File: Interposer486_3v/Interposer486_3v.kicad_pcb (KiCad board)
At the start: 2 copper layers, 48.3 x 52.1 mm, 170 parts, among them J1 WB/~WT, J2 CLKMUL

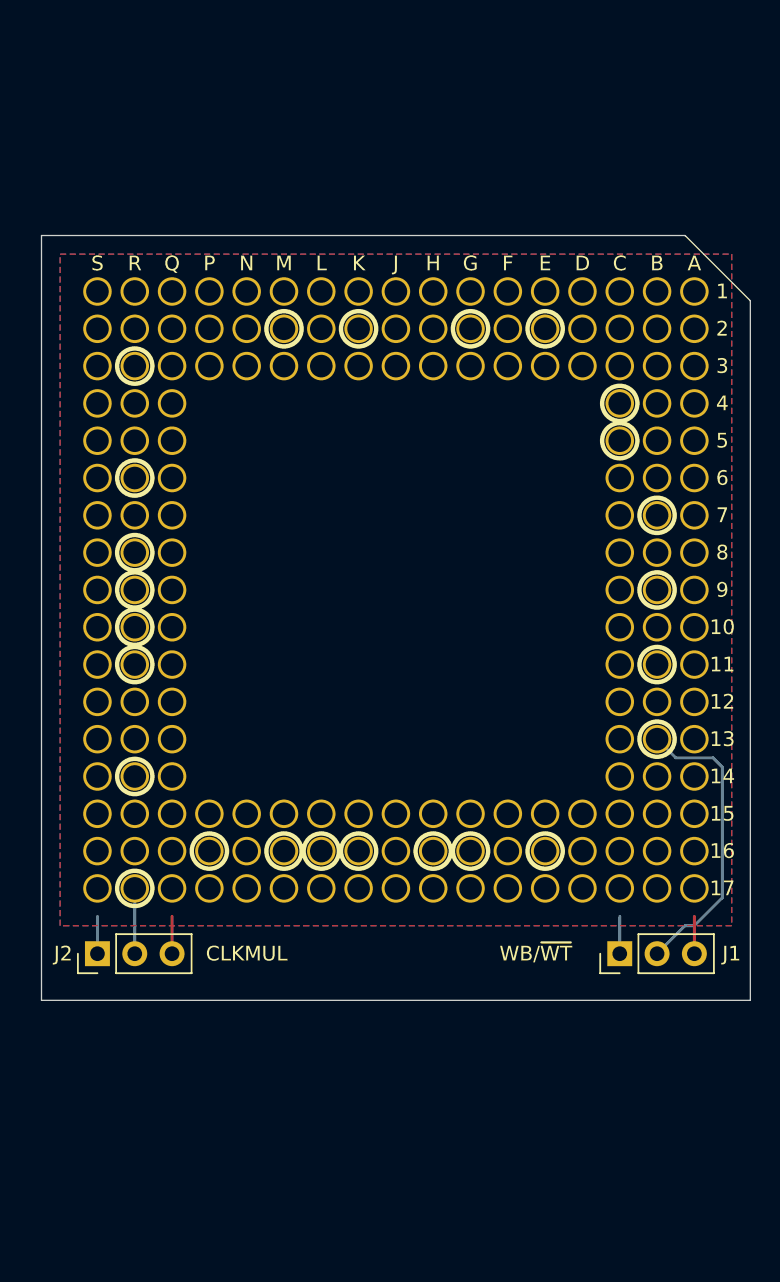
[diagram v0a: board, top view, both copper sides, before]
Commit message: Completed first pass of layout of 486 3v interposer.
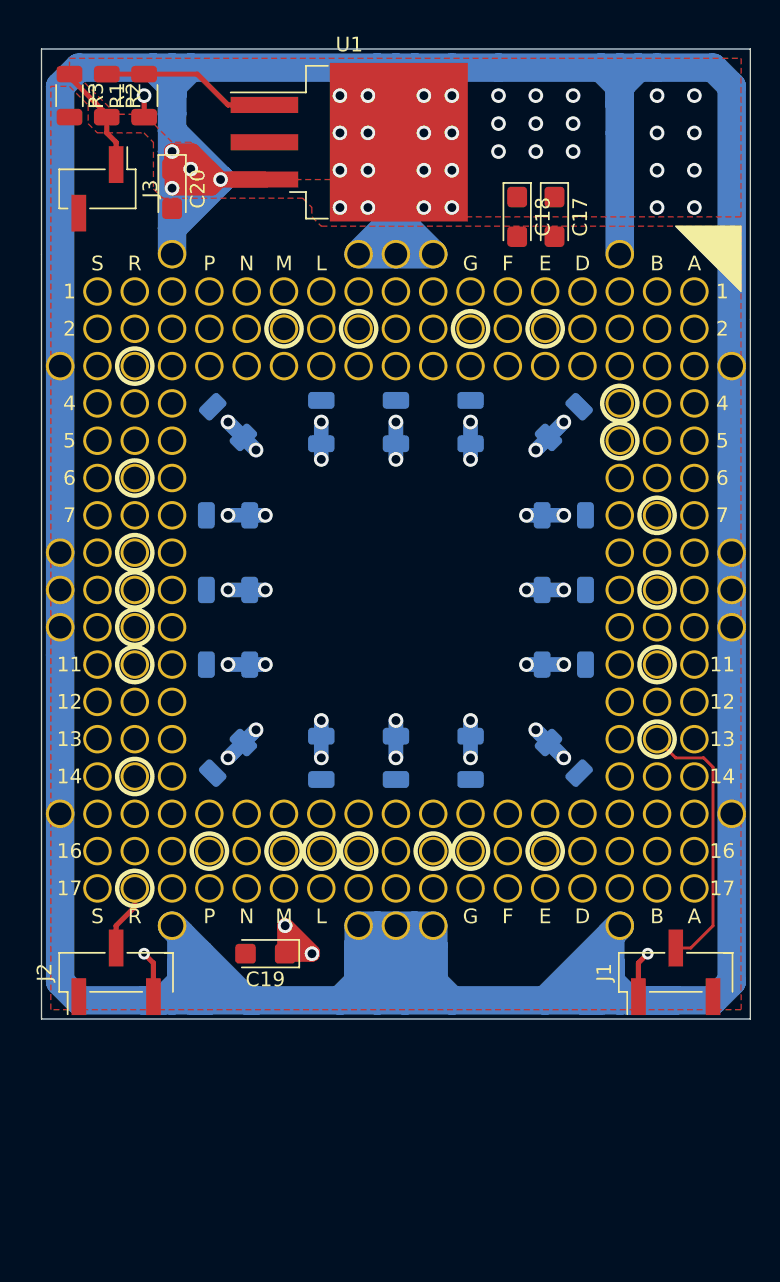
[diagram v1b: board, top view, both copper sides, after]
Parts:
- added C1: 0.1uF, Capacitor_SMD:C_1206_3216Metric, B.Cu at (146.1, 69.8)
- added C10: 0.1uF, Capacitor_SMD:C_1206_3216Metric, B.Cu at (162.6, 92.7)
- added C11: 0.1uF, Capacitor_SMD:C_1206_3216Metric, B.Cu at (157.5, 92.7)
- added C12: 0.1uF, Capacitor_SMD:C_1206_3216Metric, B.Cu at (152.4, 92.7)
- added C13: 0.1uF, Capacitor_SMD:C_1206_3216Metric, B.Cu at (146.1, 92.7)
- added C14: 0.1uF, Capacitor_SMD:C_1206_3216Metric, B.Cu at (146.1, 86.4)
- added C15: 0.1uF, Capacitor_SMD:C_1206_3216Metric, B.Cu at (146.1, 81.3)
- added C16: 0.1uF, Capacitor_SMD:C_1206_3216Metric, B.Cu at (146.1, 76.2)
- added C17: 10uF, Capacitor_Tantalum_SMD:CP_EIA-3216-10_Kemet-I, F.Cu at (168.3, 55.9)
- added C18: 10uF, Capacitor_Tantalum_SMD:CP_EIA-3216-10_Kemet-I, F.Cu at (165.7, 55.9)
- added C19: 10uF, Capacitor_Tantalum_SMD:CP_EIA-3216-10_Kemet-I, F.Cu at (148.6, 106.0)
- added C2: 0.1uF, Capacitor_SMD:C_1206_3216Metric, B.Cu at (152.4, 69.8)
- added C20: 10uF, Capacitor_Tantalum_SMD:CP_EIA-3216-10_Kemet-I, F.Cu at (142.2, 54.0)
- added C3: 0.1uF, Capacitor_SMD:C_1206_3216Metric, B.Cu at (157.5, 69.8)
- added C4: 0.1uF, Capacitor_SMD:C_1206_3216Metric, B.Cu at (162.6, 69.8)
- added C5: 0.1uF, Capacitor_SMD:C_1206_3216Metric, B.Cu at (168.9, 69.8)
- added C6: 0.1uF, Capacitor_SMD:C_1206_3216Metric, B.Cu at (168.9, 76.2)
- added C7: 0.1uF, Capacitor_SMD:C_1206_3216Metric, B.Cu at (168.9, 81.3)
- added C8: 0.1uF, Capacitor_SMD:C_1206_3216Metric, B.Cu at (168.9, 86.4)
- added C9: 0.1uF, Capacitor_SMD:C_1206_3216Metric, B.Cu at (168.9, 92.7)
- added HAA10: ???, 00Custom:MachinePinHole, F.Cu at (180.3, 83.8)
- added HAA15: ???, 00Custom:MachinePinHole, F.Cu at (180.3, 96.5)
- added HAA3: ???, 00Custom:MachinePinHole, F.Cu at (180.3, 66.0)
- added HAA8: ??, 00Custom:MachinePinHole, F.Cu at (180.3, 78.7)
- added HAA9: ???, 00Custom:MachinePinHole, F.Cu at (180.3, 81.3)
- added HC0: ???, 00Custom:MachinePinHole, F.Cu at (172.7, 58.4)
- added HC18: ???, 00Custom:MachinePinHole, F.Cu at (172.7, 104.1)
- added HH0: ???, 00Custom:MachinePinHole, F.Cu at (160.0, 58.4)
- added HH18: ???, 00Custom:MachinePinHole, F.Cu at (160.0, 104.1)
- added HJ0: ???, 00Custom:MachinePinHole, F.Cu at (157.5, 58.4)
- added HJ18: ???, 00Custom:MachinePinHole, F.Cu at (157.5, 104.1)
- added HK0: ???, 00Custom:MachinePinHole, F.Cu at (154.9, 58.4)
- added HK18: ???, 00Custom:MachinePinHole, F.Cu at (154.9, 104.1)
- added HQ0: ???, 00Custom:MachinePinHole, F.Cu at (142.2, 58.4)
- added HQ18: ???, 00Custom:MachinePinHole, F.Cu at (142.2, 104.1)
- added HSS10: ???, 00Custom:MachinePinHole, F.Cu at (134.6, 83.8)
- added HSS15: ???, 00Custom:MachinePinHole, F.Cu at (134.6, 96.5)
- added HSS3: ???, 00Custom:MachinePinHole, F.Cu at (134.6, 66.0)
- added HSS8: ???, 00Custom:MachinePinHole, F.Cu at (134.6, 78.7)
- added HSS9: ???, 00Custom:MachinePinHole, F.Cu at (134.6, 81.3)
- added J3: V Select, Connector_PinHeader_2.54mm:PinHeader_1x02_P2.54mm_Vertical_SMD_Pin1Left, F.Cu at (137.2, 54.0)
- added R1: 121R, Resistor_SMD:R_1206_3216Metric, F.Cu at (140.3, 47.6)
- added R2: 200R, Resistor_SMD:R_1206_3216Metric, F.Cu at (137.8, 47.6)
- added R3: 12R, Resistor_SMD:R_1206_3216Metric, F.Cu at (135.3, 47.6)
- added U1: LT1085-ADJ, Package_TO_SOT_SMD:TO-263-3_TabPin2, F.Cu at (154.3, 50.8)
- J1, J2: footprint Connector_PinHeader_2.54mm:PinHeader_1x03_P2.54mm_Vertical -> Connector_PinHeader_2.54mm:PinHeader_1x03_P2.54mm_Vertical_SMD_Pin1Left
- moved J1 4.02 mm to (176.5, 107.3)
- moved J2 1.80 mm to (138.4, 107.3)
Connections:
- J2 pad 1: VCC -> VSS
- J2 pad 3: VSS -> VCC
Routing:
- net +5V: track 0.00 -> 408.2 mm, vias 0 -> 4
- net VSS: track 5.08 -> 41.3 mm, vias 0 -> 32
- net Net-(R1-Pad2): track 0.00 -> 11.6 mm
- net VCC: track 5.08 -> 14.1 mm, vias 0 -> 38
- net Net-(J3-Pad1): track 0.00 -> 7.47 mm
- net WB_~WT: track 20.1 -> 18.6 mm
- added copper zone on F.Cu, net VCC
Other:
- board size 48.3 x 52.1 mm -> 48.3 x 66 mm
- net class Power added: clearance 0.2, trace_width 1, via_dia 1, via_drill 0.6
- board text removed: "10"
- board text removed: "15"
- board text removed: "3"
- board text removed: "8"
- board text removed: "9"
- board text removed: "C"
- board text removed: "H"
- board text removed: "J"
- board text removed: "K"
- board text removed: "Q"

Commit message: Jig hole wip
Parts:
- added HDT1: ???, 00Custom:MachinePinHole, F.Cu at (139.7, 114.3)
- added HDT10: ???, 00Custom:MachinePinHole, F.Cu at (152.4, 116.8)
- added HDT11: ???, 00Custom:MachinePinHole, F.Cu at (157.5, 116.8)
- added HDT12: ???, 00Custom:MachinePinHole, F.Cu at (162.6, 116.8)
- added HDT13: ???, 00Custom:MachinePinHole, F.Cu at (167.6, 116.8)
- added HDT14: ???, 00Custom:MachinePinHole, F.Cu at (172.7, 116.8)
- added HDT15: ???, 00Custom:MachinePinHole, F.Cu at (139.7, 119.4)
- added HDT16: ???, 00Custom:MachinePinHole, F.Cu at (144.8, 119.4)
- added HDT17: ???, 00Custom:MachinePinHole, F.Cu at (149.9, 119.4)
- added HDT18: ???, 00Custom:MachinePinHole, F.Cu at (154.9, 119.4)
- added HDT19: ???, 00Custom:MachinePinHole, F.Cu at (160.0, 119.4)
- added HDT2: ???, 00Custom:MachinePinHole, F.Cu at (144.8, 114.3)
- added HDT20: ???, 00Custom:MachinePinHole, F.Cu at (165.1, 119.4)
- added HDT21: ???, 00Custom:MachinePinHole, F.Cu at (170.2, 119.4)
- added HDT22: ???, 00Custom:MachinePinHole, F.Cu at (142.2, 121.9)
- added HDT23: ???, 00Custom:MachinePinHole, F.Cu at (147.3, 121.9)
- added HDT24: ???, 00Custom:MachinePinHole, F.Cu at (152.4, 121.9)
- added HDT25: ???, 00Custom:MachinePinHole, F.Cu at (157.5, 121.9)
- added HDT26: ???, 00Custom:MachinePinHole, F.Cu at (162.6, 121.9)
- added HDT27: ???, 00Custom:MachinePinHole, F.Cu at (167.6, 121.9)
- added HDT28: ???, 00Custom:MachinePinHole, F.Cu at (172.7, 121.9)
- added HDT3: ???, 00Custom:MachinePinHole, F.Cu at (149.9, 114.3)
- added HDT4: ???, 00Custom:MachinePinHole, F.Cu at (154.9, 114.3)
- added HDT5: ???, 00Custom:MachinePinHole, F.Cu at (160.0, 114.3)
- added HDT6: ???, 00Custom:MachinePinHole, F.Cu at (165.1, 114.3)
- added HDT7: ???, 00Custom:MachinePinHole, F.Cu at (170.2, 114.3)
- added HDT8: ???, 00Custom:MachinePinHole, F.Cu at (142.2, 116.8)
- added HDT9: ???, 00Custom:MachinePinHole, F.Cu at (147.3, 116.8)

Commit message: Finished first pass of 486 3v interposer.
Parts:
- moved HDT1 2.29 mm to (141.0, 116.2)
- moved HDT11 2.29 mm to (158.8, 118.7)
- moved HDT12 2.29 mm to (163.8, 118.7)
- moved HDT13 2.29 mm to (168.9, 118.7)
- moved HDT14 2.29 mm to (174.0, 118.7)
- moved HDT15 2.29 mm to (141.0, 121.3)
- moved HDT16 2.29 mm to (146.1, 121.3)
- moved HDT18 2.29 mm to (156.2, 121.3)
- moved HDT2 2.29 mm to (146.1, 116.2)
- moved HDT20 2.29 mm to (166.4, 121.3)
- moved HDT23 2.29 mm to (148.6, 123.8)
- moved HDT25 2.29 mm to (158.8, 123.8)
- moved HDT26 2.29 mm to (163.8, 123.8)
- moved HDT27 2.29 mm to (168.9, 123.8)
- moved HDT28 2.29 mm to (174.0, 123.8)
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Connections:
- HDT1 pad 1: (no net) -> VSS
- HDT10 pad 1: (no net) -> VSS
- HDT11 pad 1: (no net) -> VSS
- HDT12 pad 1: (no net) -> VSS
- HDT13 pad 1: (no net) -> VSS
- HDT14 pad 1: (no net) -> VSS
- HDT15 pad 1: (no net) -> VSS
- HDT16 pad 1: (no net) -> VSS
- HDT17 pad 1: (no net) -> VSS
- HDT18 pad 1: (no net) -> VSS
- HDT19 pad 1: (no net) -> VSS
- HDT2 pad 1: (no net) -> VSS
- HDT20 pad 1: (no net) -> VSS
- HDT21 pad 1: (no net) -> VSS
- HDT22 pad 1: (no net) -> VSS
- HDT23 pad 1: (no net) -> VSS
- HDT24 pad 1: (no net) -> VSS
- HDT25 pad 1: (no net) -> VSS
- HDT26 pad 1: (no net) -> VSS
- HDT27 pad 1: (no net) -> VSS
- HDT28 pad 1: (no net) -> VSS
- HDT3 pad 1: (no net) -> VSS
- HDT4 pad 1: (no net) -> VSS
- HDT5 pad 1: (no net) -> VSS
- HDT6 pad 1: (no net) -> VSS
- HDT7 pad 1: (no net) -> VSS
- HDT8 pad 1: (no net) -> VSS
- HDT9 pad 1: (no net) -> VSS
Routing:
- net VSS: track 41.3 -> 52.7 mm
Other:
- board size 48.3 x 66 mm -> 48.3 x 81.9 mm
- board text added: "121R 1206 200R 1206 20R 1206 0.1uF MLCC 1206 10uF 16v Tantalum 3216 LT1085, LD1085 or LM1085 ADJ D-PAK"
- board text added: "486 3v CPU Interposer"
- board text added: "CLKMUL"
- board text added: "It probably won't fry something special. Maybe. Who knows?"
- board text added: "OFF"
- board text added: "ON"
- board text added: "ON=3.3v OFF=3.45v"
- board text added: "R1 R2 R3 C1- C16 C17- C20 U1"
- board text added: "WB"
- board text added: "WT"
- board text added: "https://github.com/ JayesonLS/Interposer Placed into the Public Domain. Use freely and at own risk"
- board text added: "https://github.com/JayesonLS/Interposer Placed into the Public Domain. Use freely and at own risk It probably won't fry something special. Maybe. Who knows?"
